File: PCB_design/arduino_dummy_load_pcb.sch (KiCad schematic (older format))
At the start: 15 parts, among them J1 Barrel_Jack, J2 Conn_02x08_Odd_Even, U1 MCP3208

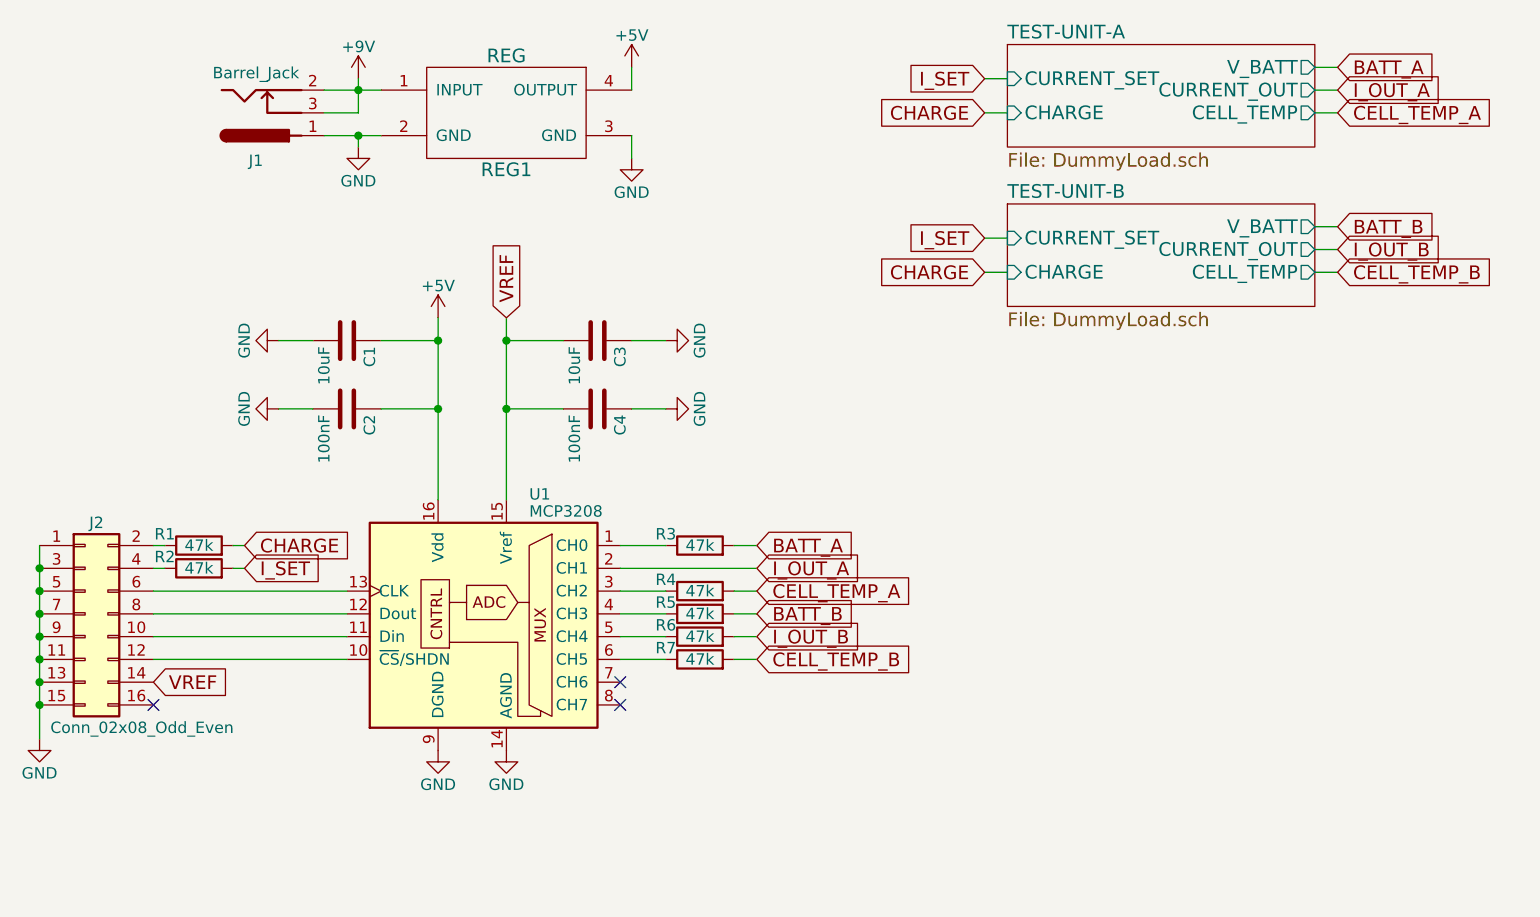
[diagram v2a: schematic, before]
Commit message: added readme (needs lots of work), basically final PCB
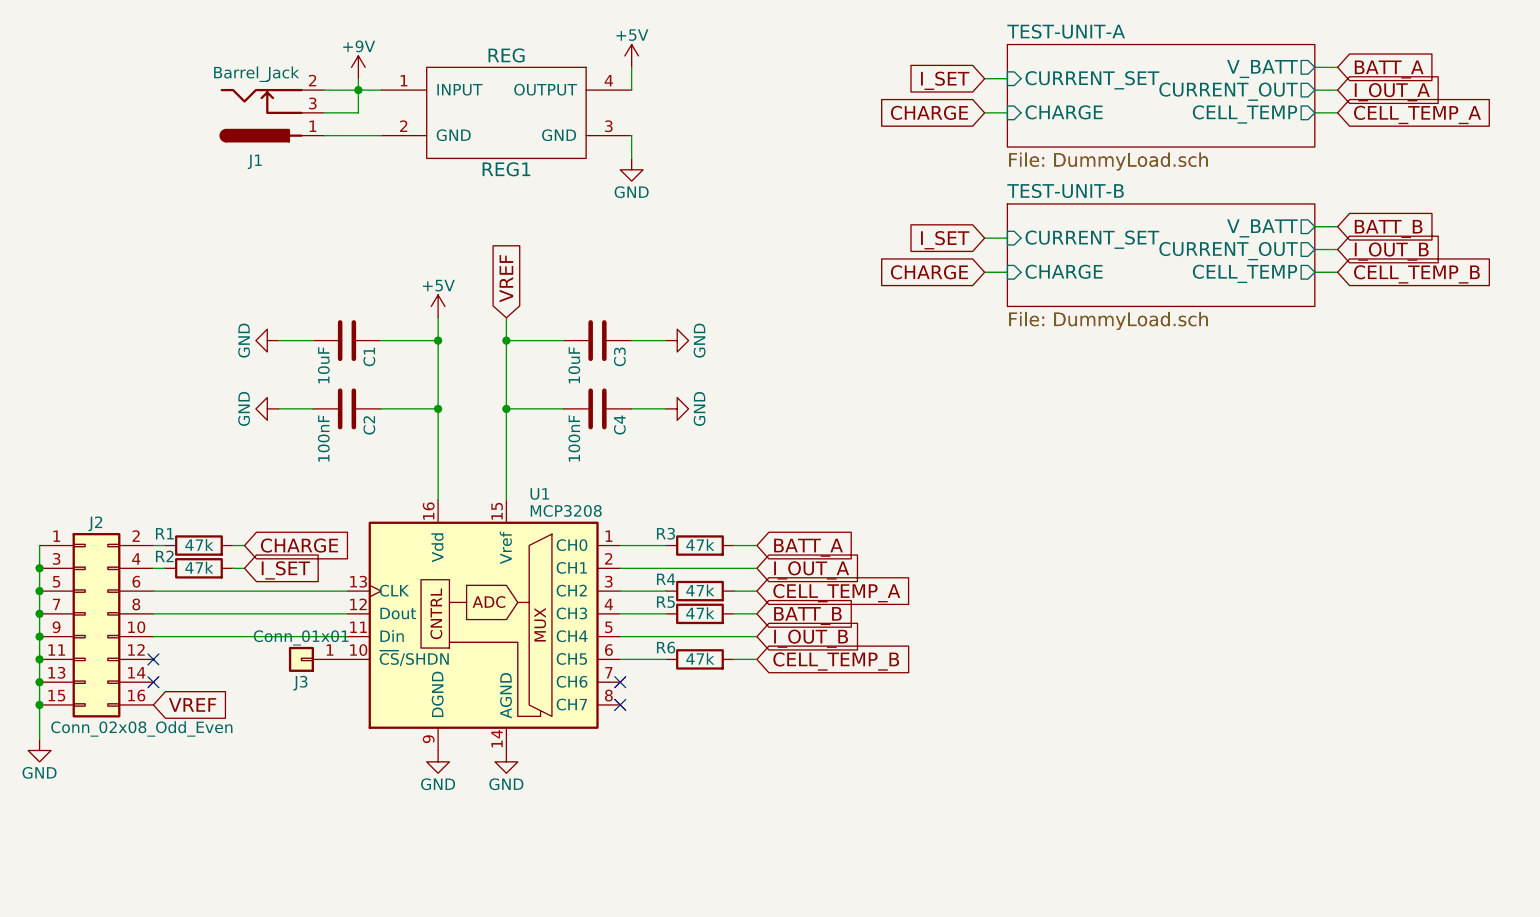
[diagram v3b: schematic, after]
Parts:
- removed R6: 47k, Resistors_SMD:R_0805_HandSoldering, symbol R
- added J3: Conn_01x01, Connectors:1pin, symbol Conn_01x01
- REG1: footprint (none) -> Library:LM2596_module
- renumbered R7 to R6
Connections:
- net GND: no longer J1.1, REG1.2 (GND)
- net I_OUT_B: now also U1.5 (CH4)
- net VREF: now also J2.16 (Pin_16); no longer J2.14 (Pin_14)
- net at U1.10 (~CS~/SHDN): now also J3.1 (Pin_1); no longer J2.12 (Pin_12)
- new net: J1.1, REG1.2 (GND)
- no-connect marks 3 -> 4
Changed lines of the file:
@@
 $EndComp
 $Comp
-L GND #PWR02
-U 1 1 59F3DB9E
-P 3000 1400
-F 0 "#PWR02" H 3000 1150 50  0001 C CNN
-F 1 "GND" H 3000 1250 50  0000 C CNN
-F 2 "" H 3000 1400 50  0001 C CNN
-F 3 "" H 3000 1400 50  0001 C CNN
-	1    3000 1400
-	1    0    0    -1
-$EndComp
-$Comp
-L +5V #PWR03
+L +5V #PWR02
 U 1 1 59F4A78A
 P 4200 1050
-F 0 "#PWR03" H 4200 900 50  0001 C CNN
+F 0 "#PWR02" H 4200 900 50  0001 C CNN
 F 1 "+5V" H 4200 1190 50  0000 C CNN
 F 2 "" H 4200 1050 50  0001 C CNN
@@
 F 0 "REG1" H 3650 1000 60  0000 C CNN
 F 1 "REG" H 3650 1500 60  0000 C CNN
-F 2 "" H 3600 1250 60  0001 C CNN
+F 2 "Library:LM2596_module" H 3600 1250 60  0001 C CNN
 F 3 "" H 3600 1250 60  0001 C CNN
 	1    3650 1250
@@
 $EndComp
 $Comp
-L GND #PWR04
+L GND #PWR03
 U 1 1 5A04F666
 P 3650 4050
-F 0 "#PWR04" H 3650 3800 50  0001 C CNN
+F 0 "#PWR03" H 3650 3800 50  0001 C CNN
 F 1 "GND" H 3650 3900 50  0000 C CNN
 F 2 "" H 3650 4050 50  0001 C CNN
@@
 $EndComp
 $Comp
-L GND #PWR05
+L GND #PWR04
 U 1 1 5A20F379
 P 1600 4000
-F 0 "#PWR05" H 1600 3750 50  0001 C CNN
+F 0 "#PWR04" H 1600 3750 50  0001 C CNN
 F 1 "GND" H 1600 3850 50  0000 C CNN
 F 2 "" H 1600 4000 50  0001 C CNN
@@
 $EndComp
 $Comp
-L R R7
+L R R6
 U 1 1 5A22951F
 P 4500 3650
-F 0 "R7" V 4550 3800 50  0000 C CNN
+F 0 "R6" V 4550 3800 50  0000 C CNN
 F 1 "47k" V 4500 3650 50  0000 C CNN
 F 2 "Resistors_SMD:R_0805_HandSoldering" V 4430 3650 50  0001 C CNN
 F 3 "" H 4500 3650 50  0001 C CNN
 	1    4500 3650
-	0    -1   -1   0
-$EndComp
-$Comp
-L R R6
-U 1 1 5A2293D0
-P 4500 3550
-F 0 "R6" V 4550 3700 50  0000 C CNN
-F 1 "47k" V 4500 3550 50  0000 C CNN
-F 2 "Resistors_SMD:R_0805_HandSoldering" V 4430 3550 50  0001 C CNN
-F 3 "" H 4500 3550 50  0001 C CNN
-	1    4500 3550
 	0    -1   -1   0
 $EndComp
@@
 $EndComp
 $Comp
-L +5V #PWR06
+L +5V #PWR05
 U 1 1 59F7FE3E
 P 3350 2150
-F 0 "#PWR06" H 3350 2000 50  0001 C CNN
+F 0 "#PWR05" H 3350 2000 50  0001 C CNN
 F 1 "+5V" H 3350 2290 50  0000 C CNN
 F 2 "" H 3350 2150 50  0001 C CNN
@@
 $EndComp
 $Comp
-L GND #PWR07
+L GND #PWR06
 U 1 1 59F80B3F
 P 3350 4050
-F 0 "#PWR07" H 3350 3800 50  0001 C CNN
+F 0 "#PWR06" H 3350 3800 50  0001 C CNN
 F 1 "GND" H 3350 3900 50  0000 C CNN
 F 2 "" H 3350 4050 50  0001 C CNN
@@
 $EndComp
 $Comp
-L GND #PWR08
+L GND #PWR07
 U 1 1 59F80CA3
 P 2650 2250
-F 0 "#PWR08" H 2650 2000 50  0001 C CNN
+F 0 "#PWR07" H 2650 2000 50  0001 C CNN
 F 1 "GND" H 2650 2100 50  0000 C CNN
 F 2 "" H 2650 2250 50  0001 C CNN
@@
 $EndComp
 $Comp
-L GND #PWR09
+L GND #PWR08
 U 1 1 59FD1D7D
 P 4200 1450
-F 0 "#PWR09" H 4200 1200 50  0001 C CNN
+F 0 "#PWR08" H 4200 1200 50  0001 C CNN
 F 1 "GND" H 4200 1300 50  0000 C CNN
 F 2 "" H 4200 1450 50  0001 C CNN
@@
 	1    0    0    -1
 $EndComp
-Wire Wire Line
-	3000 1100 3000 1250
-Wire Wire Line
-	3000 1250 2850 1250
-Connection ~ 3000 1150
-Wire Wire Line
-	4650 3150 4750 3150
-Wire Wire Line
-	4150 3250 4750 3250
-Wire Wire Line
-	4200 1350 4200 1450
-Wire Wire Line
-	4200 1050 4200 1150
-Connection ~ 1600 3850
-Connection ~ 1600 3650
-Connection ~ 1600 3450
-Connection ~ 1600 3250
-Connection ~ 1600 3350
-Connection ~ 1600 3550
-Connection ~ 1600 3750
-Wire Wire Line
-	4650 3350 4750 3350
-Wire Wire Line
-	1600 3150 1600 4000
-Wire Wire Line
-	2450 3150 2500 3150
-Wire Wire Line
-	2500 3250 2450 3250
-Wire Wire Line
-	4150 3150 4350 3150
-Wire Wire Line
-	4150 3450 4350 3450
-Wire Wire Line
-	4150 3550 4350 3550
-Wire Wire Line
-	4150 3650 4350 3650
-Wire Wire Line
-	4150 3350 4350 3350
-Wire Wire Line
-	3350 2150 3350 2950
-Wire Wire Line
-	3100 2250 3350 2250
-Connection ~ 3350 2250
-Wire Wire Line
-	2650 2250 2800 2250
-Wire Wire Line
-	3000 1400 3000 1350
-Connection ~ 3000 1350
-Wire Wire Line
-	2850 1150 3100 1150
-Wire Wire Line
-	2850 1350 3100 1350
-Wire Wire Line
-	2100 3150 2150 3150
-Wire Wire Line
-	2100 3250 2150 3250
-Wire Wire Line
-	2100 3350 2950 3350
-Wire Wire Line
-	2950 3450 2100 3450
-Wire Wire Line
-	2100 3550 2950 3550
-Wire Wire Line
-	2950 3650 2100 3650
 $Sheet
 S 5850 950  1350 450
@@
 	0    -1   -1   0
 $EndComp
-NoConn ~ 2100 3850
 Text GLabel 5750 1250 0    60   Input ~ 0
 CHARGE
-Wire Wire Line
-	5750 1250 5850 1250
 Text GLabel 5750 1100 0    60   Input ~ 0
 I_SET
-Wire Wire Line
-	5850 1100 5750 1100
 Text GLabel 7300 1250 2    60   Input ~ 0
 CELL_TEMP_A
-Wire Wire Line
-	7200 1250 7300 1250
 Text GLabel 7300 1150 2    60   Input ~ 0
 I_OUT_A
-Wire Wire Line
-	7300 1150 7200 1150
 Text GLabel 7300 1050 2    60   Input ~ 0
 BATT_A
-Wire Wire Line
-	7300 1050 7200 1050
-Wire Wire Line
-	4650 3450 4750 3450
-Wire Wire Line
-	4750 3550 4650 3550
-Wire Wire Line
-	4650 3650 4750 3650
 $Sheet
 S 5850 1650 1350 450
@@
 Text GLabel 5750 1950 0    60   Input ~ 0
 CHARGE
-Wire Wire Line
-	5750 1950 5850 1950
 Text GLabel 5750 1800 0    60   Input ~ 0
 I_SET
-Wire Wire Line
-	5850 1800 5750 1800
 Text GLabel 7300 1950 2    60   Input ~ 0
 CELL_TEMP_B
-Wire Wire Line
-	7200 1950 7300 1950
 Text GLabel 7300 1850 2    60   Input ~ 0
 I_OUT_B
-Wire Wire Line
-	7300 1850 7200 1850
 Text GLabel 7300 1750 2    60   Input ~ 0
 BATT_B
-Wire Wire Line
-	7300 1750 7200 1750
 Text GLabel 3650 2150 1    60   Input ~ 0
 VREF
-Text GLabel 2100 3750 2    60   Input ~ 0
+Text GLabel 2100 3850 2    60   Input ~ 0
 VREF
-Wire Wire Line
-	3650 2150 3650 2950
 $Comp
 L C C2
@@
 	0    1    1    0
 $EndComp
-Wire Wire Line
-	3100 2550 3350 2550
-Connection ~ 3650 2550
-$Comp
-L GND #PWR010
+$Comp
+L GND #PWR09
 U 1 1 5A04B5B5
 P 2650 2550
-F 0 "#PWR010" H 2650 2300 50  0001 C CNN
+F 0 "#PWR09" H 2650 2300 50  0001 C CNN
 F 1 "GND" H 2650 2400 50  0000 C CNN
 F 2 "" H 2650 2550 50  0001 C CNN
@@
 	0    1    1    0
 $EndComp
-Wire Wire Line
-	2650 2550 2800 2550
 $Comp
 L C C3
@@
 $EndComp
 $Comp
-L GND #PWR011
+L GND #PWR010
 U 1 1 5A04C217
 P 4350 2250
-F 0 "#PWR011" H 4350 2000 50  0001 C CNN
+F 0 "#PWR010" H 4350 2000 50  0001 C CNN
 F 1 "GND" H 4350 2100 50  0000 C CNN
 F 2 "" H 4350 2250 50  0001 C CNN
@@
 	0    -1   -1   0
 $EndComp
-Wire Wire Line
-	3650 2250 3900 2250
-Wire Wire Line
-	4200 2250 4350 2250
-Connection ~ 3650 2250
 $Comp
 L C C4
@@
 	0    1    1    0
 $EndComp
-Wire Wire Line
-	3900 2550 3650 2550
-$Comp
-L GND #PWR012
+$Comp
+L GND #PWR011
 U 1 1 5A04CF95
 P 4350 2550
-F 0 "#PWR012" H 4350 2300 50  0001 C CNN
+F 0 "#PWR011" H 4350 2300 50  0001 C CNN
 F 1 "GND" H 4350 2400 50  0000 C CNN
 F 2 "" H 4350 2550 50  0001 C CNN
@@
 	0    -1   -1   0
 $EndComp
-Wire Wire Line
-	4200 2550 4350 2550
-Connection ~ 3350 2550
 Text GLabel 4750 3550 2    60   Input ~ 0
 I_OUT_B
 NoConn ~ 4150 3750
 NoConn ~ 4150 3850
+Wire Wire Line
+	3000 1100 3000 1250
+Wire Wire Line
+	3000 1250 2850 1250
+Connection ~ 3000 1150
+Wire Wire Line
+	4650 3150 4750 3150
+Wire Wire Line
+	4150 3250 4750 3250
+Wire Wire Line
+	4200 1350 4200 1450
+Wire Wire Line
+	4200 1050 4200 1150
+Connection ~ 1600 3850
+Connection ~ 1600 3650
+Connection ~ 1600 3450
+Connection ~ 1600 3250
+Connection ~ 1600 3350
+Connection ~ 1600 3550
+Connection ~ 1600 3750
+Wire Wire Line
+	4650 3350 4750 3350
+Wire Wire Line
+	1600 3150 1600 4000
+Wire Wire Line
+	2450 3150 2500 3150
+Wire Wire Line
+	2500 3250 2450 3250
+Wire Wire Line
+	4150 3150 4350 3150
+Wire Wire Line
+	4150 3450 4350 3450
+Wire Wire Line
+	4150 3550 4750 3550
+Wire Wire Line
+	4150 3650 4350 3650
+Wire Wire Line
+	4150 3350 4350 3350
+Wire Wire Line
+	3350 2150 3350 2950
+Wire Wire Line
+	3100 2250 3350 2250
+Connection ~ 3350 2250
+Wire Wire Line
+	2650 2250 2800 2250
+Wire Wire Line
+	2850 1150 3100 1150
+Wire Wire Line
+	2100 3150 2150 3150
+Wire Wire Line
+	2100 3250 2150 3250
+Wire Wire Line
+	2100 3350 2950 3350
+Wire Wire Line
+	2950 3450 2100 3450
+Wire Wire Line
+	2100 3550 2950 3550
+Wire Wire Line
+	5750 1250 5850 1250
+Wire Wire Line
+	5850 1100 5750 1100
+Wire Wire Line
+	7200 1250 7300 1250
+Wire Wire Line
+	7300 1150 7200 1150
+Wire Wire Line
+	7300 1050 7200 1050
+Wire Wire Line
+	4650 3450 4750 3450
+Wire Wire Line
+	4650 3650 4750 3650
+Wire Wire Line
+	5750 1950 5850 1950
+Wire Wire Line
+	5850 1800 5750 1800
+Wire Wire Line
+	7200 1950 7300 1950
+Wire Wire Line
+	7300 1850 7200 1850
+Wire Wire Line
+	7300 1750 7200 1750
+Wire Wire Line
+	3650 2150 3650 2950
+Wire Wire Line
+	3100 2550 3350 2550
+Connection ~ 3650 2550
+Wire Wire Line
+	2650 2550 2800 2550
+Wire Wire Line
+	3650 2250 3900 2250
+Wire Wire Line
+	4200 2250 4350 2250
+Connection ~ 3650 2250
+Wire Wire Line
+	3900 2550 3650 2550
+Wire Wire Line
+	4200 2550 4350 2550
+Connection ~ 3350 2550
+Wire Wire Line
+	2850 1350 3100 1350
+$Comp
+L Conn_01x01 J3
+U 1 1 5A262B19
+P 2750 3650
+F 0 "J3" H 2750 3750 50  0000 C CNN
+F 1 "Conn_01x01" H 2750 3550 50  0000 C CNN
+F 2 "Connectors:1pin" H 2750 3650 50  0001 C CNN
+F 3 "" H 2750 3650 50  0001 C CNN
+	1    2750 3650
+	-1   0    0    1
+$EndComp
+NoConn ~ 2100 3650
+NoConn ~ 2100 3750
 $EndSCHEMATC

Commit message: adding to unstable branch
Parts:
- J1: footprint Connectors:JACK_ALIM -> Library:CUI-PJ-002AH-SMT_dc-barrel-jack
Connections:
- net +9V: now also J1.1; no longer J1.2, J1.3
- net at REG1.2 (GND): now also J1.2, J1.3; no longer J1.1
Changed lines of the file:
@@
 F 0 "J1" H 2550 1460 50  0000 C CNN
 F 1 "Barrel_Jack" H 2550 1075 50  0000 C CNN
-F 2 "Connectors:JACK_ALIM" H 2600 1210 50  0001 C CNN
+F 2 "Library:CUI-PJ-002AH-SMT_dc-barrel-jack" H 2600 1210 50  0001 C CNN
 F 3 "" H 2600 1210 50  0001 C CNN
 	1    2550 1250
-	1    0    0    1
+	1    0    0    -1
 $EndComp
 $Comp
@@
 NoConn ~ 4150 3750
 NoConn ~ 4150 3850
-Wire Wire Line
-	3000 1100 3000 1250
-Wire Wire Line
-	3000 1250 2850 1250
 Connection ~ 3000 1150
 Wire Wire Line
@@
 NoConn ~ 2100 3650
 NoConn ~ 2100 3750
+Wire Wire Line
+	3000 1150 3000 1100
+Wire Wire Line
+	3000 1250 2850 1250
+Wire Wire Line
+	3000 1250 3000 1350
+Connection ~ 3000 1350
 $EndSCHEMATC
